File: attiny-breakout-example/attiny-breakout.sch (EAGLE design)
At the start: 14 parts, among them J1 AVR_SPI_PROG_3X2NS, J2 CONN-11752, U1 3.3V/150mA

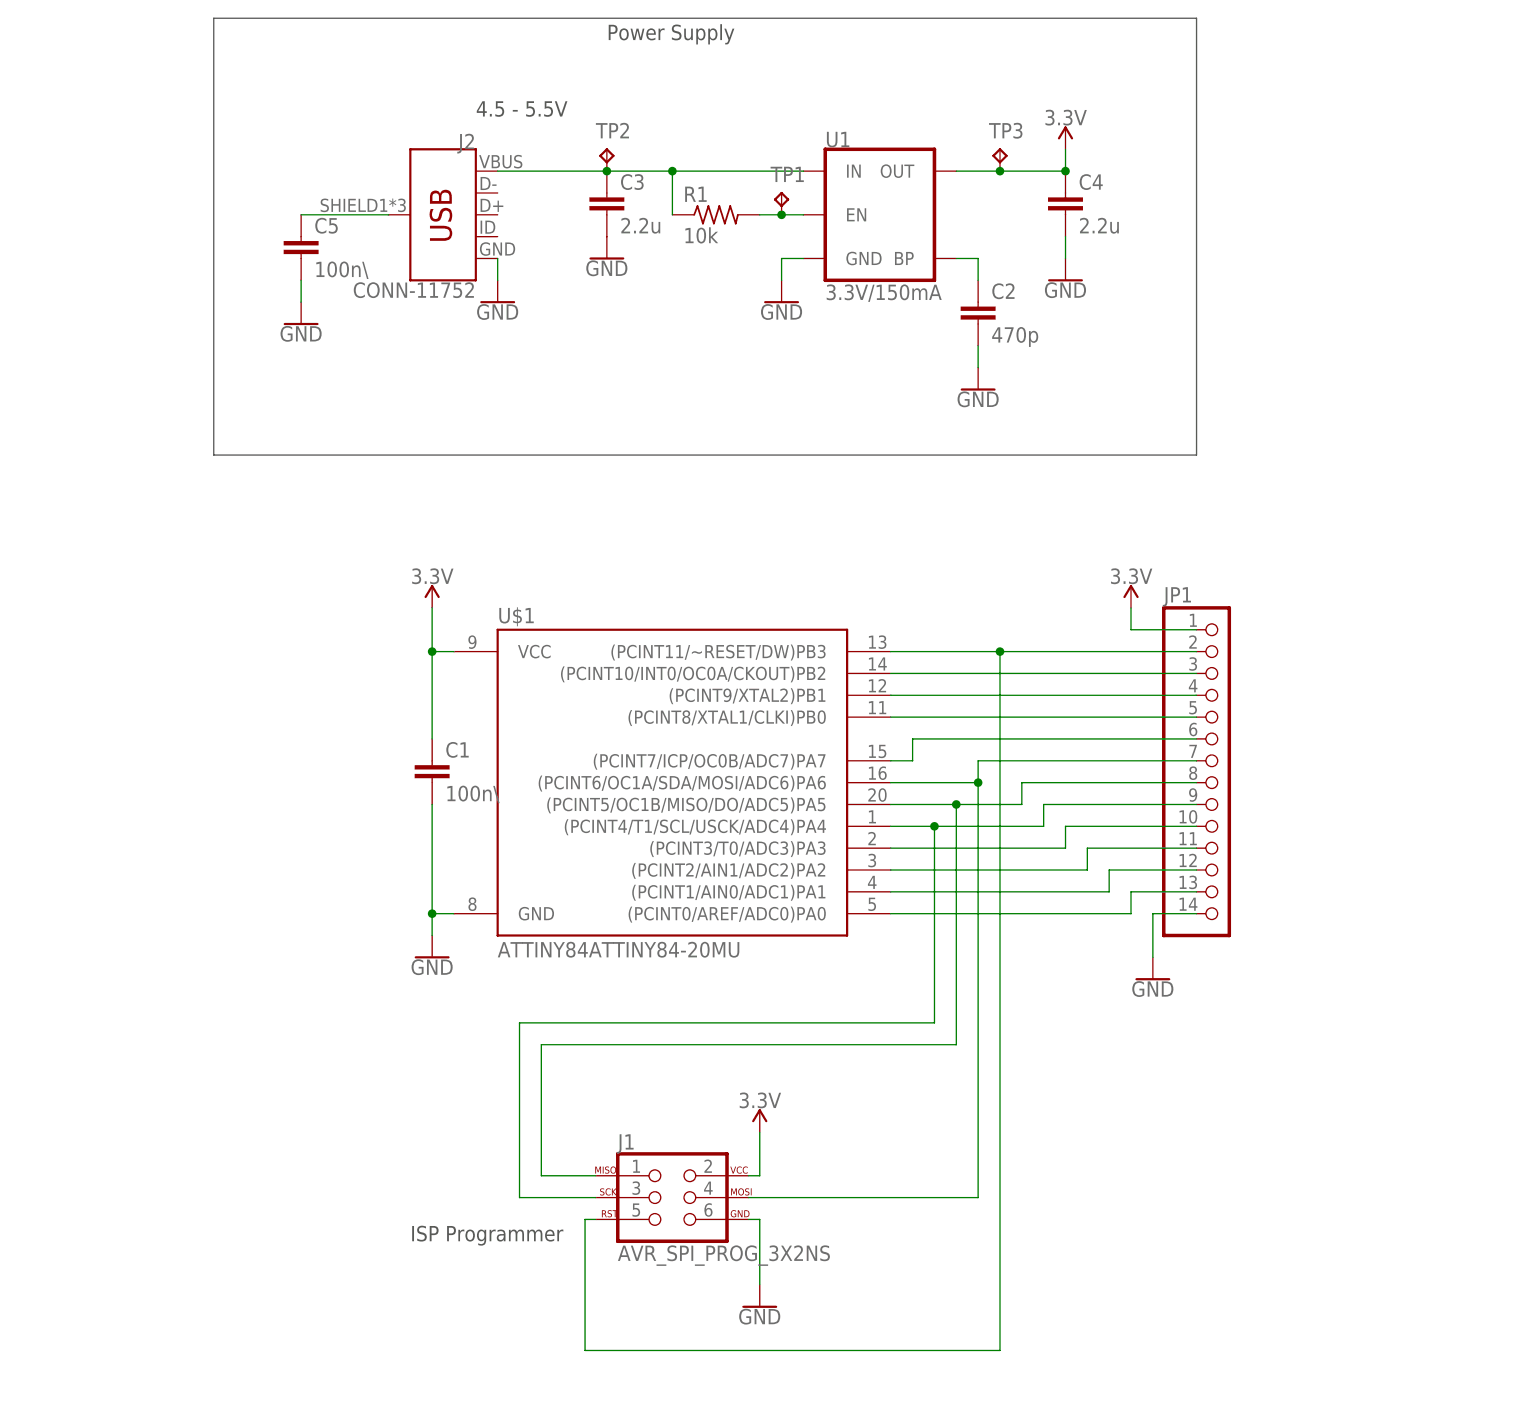
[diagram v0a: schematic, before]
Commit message: Latest bits of the attiny breakout board, and the color sensors library.
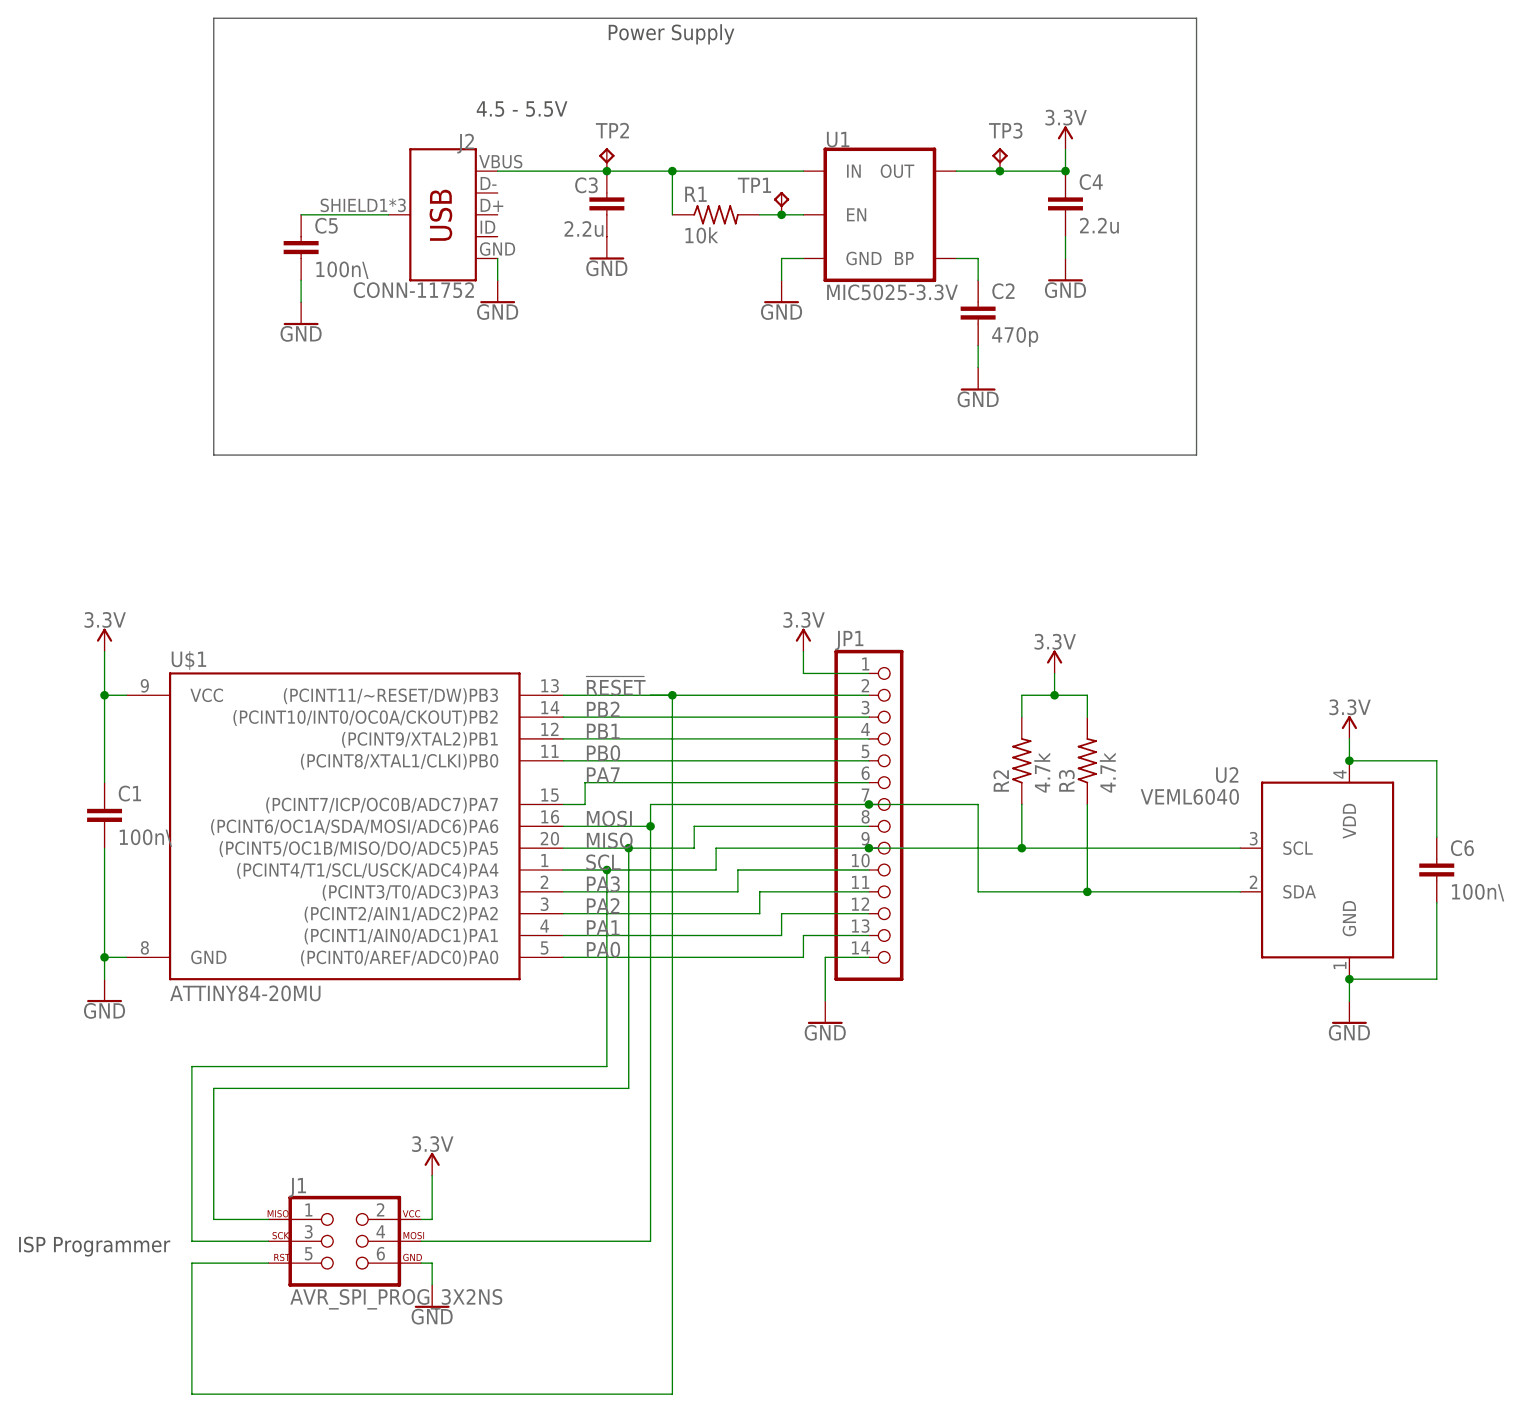
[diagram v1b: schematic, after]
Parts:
- added C6: 100n\, rcl:C-EUC0805
- added R2, R3: 4.7k, rcl:R-US_R0805
- added U2: VEML6040, color-sensors:VEML6040
- U$1: value ATTINY84ATTINY84-20MU -> ATTINY84-20MU
- U1: value 3.3V/150mA -> MIC5025-3.3V
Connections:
- net N$10 renamed PB0
- net N$11 renamed PA7
- net N$12 renamed PA3
- net N$13 renamed PA2
- net N$14 renamed PA1
- net N$15 renamed PA0
- net N$3 renamed MISO
- net N$4 renamed !RESET
- net N$8 renamed PB2
- net N$9 renamed PB1
- removed net N$1: J1.3, JP1.9, U$1.(PCINT4/T1/SCL/USCK/ADC4)PA4
- removed net N$2: J1.4, JP1.7, U$1.(PCINT6/OC1A/SDA/MOSI/ADC6)PA6
- new net MOSI: J1.4, JP1.7, R3.1, U$1.(PCINT6/OC1A/SDA/MOSI/ADC6)PA6, U2.SDA
- new net SCL: J1.3, JP1.9, R2.1, U$1.(PCINT4/T1/SCL/USCK/ADC4)PA4, U2.SCL
- net 3.3V: now also C6.1, R2.2, R3.2, U2.VDD
- net GND: now also C6.2, U2.GND
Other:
- moved on the sheet: C1, J1, JP1, U$1

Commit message: Not sure why this isn't committed, so here you go.
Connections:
- net N$6 renamed EN
- net N$7 renamed BP
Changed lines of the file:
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@@
 <setting verticaltext="up"/>
 </settings>
-<grid distance="0.05" unitdist="inch" unit="inch" style="lines" multiple="2" display="yes" altdistance="0.01" altunitdist="inch" altunit="inch"/>
+<grid distance="0.1" unitdist="inch" unit="inch" style="lines" multiple="1" display="no" altdistance="0.01" altunitdist="inch" altunit="inch"/>
 <layers>
 <layer number="1" name="Top" color="4" fill="1" visible="no" active="no"/>
@@
 </segment>
 </net>
-<net name="N$6" class="0">
+<net name="EN" class="0">
 <segment>
 <pinref part="R1" gate="G$1" pin="2"/>
@@
 </segment>
 </net>
-<net name="N$7" class="0">
+<net name="BP" class="0">
 <segment>
 <pinref part="U1" gate="U1" pin="BP"/>
